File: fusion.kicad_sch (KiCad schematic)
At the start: 67 parts, among them J1 Conn_01x04_Female, J2 USB_C_Receptacle_USB2.0, J3 Conn_02x10_Odd_Even, J4 Conn_02x10_Odd_Even, K1 KEY, K10 KEY, K11 KEY, K12 KEY, K13 KEY, K14 KEY, K15 KEY, K16 KEY, K17 KEY, K18 KEY, K19 KEY, K2 KEY, K20 KEY, K21 KEY, K22 KEY, K23 KEY, K24 KEY, K25 KEY, K26 KEY, K27 KEY, K28 KEY, K29 KEY, K3 KEY, K30 KEY, K31 KEY, K32 KEY, K33 KEY, K34 KEY, K35 KEY, K36 KEY, K37 KEY, K38 KEY, K4 KEY, K5 KEY, K6 KEY, K7 KEY, K8 KEY, K9 KEY, SW1 SW_Push, U1 Holyiot_18010, U2 MT25QL128ABA1ESE, U3 BQ24075, U4 XC6220B331MR, U5 LN4913

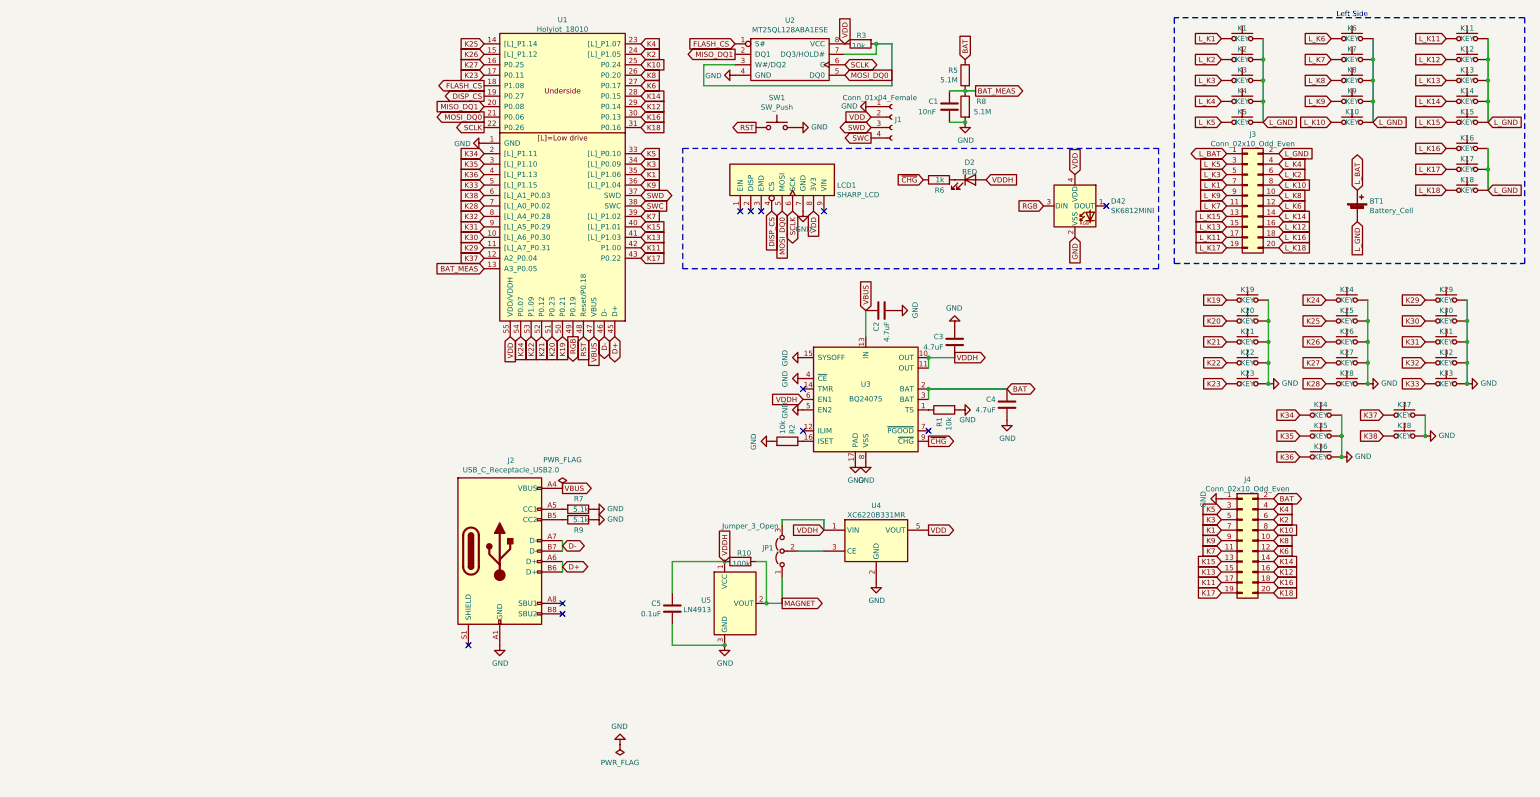
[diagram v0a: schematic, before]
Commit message: fpc and hinges
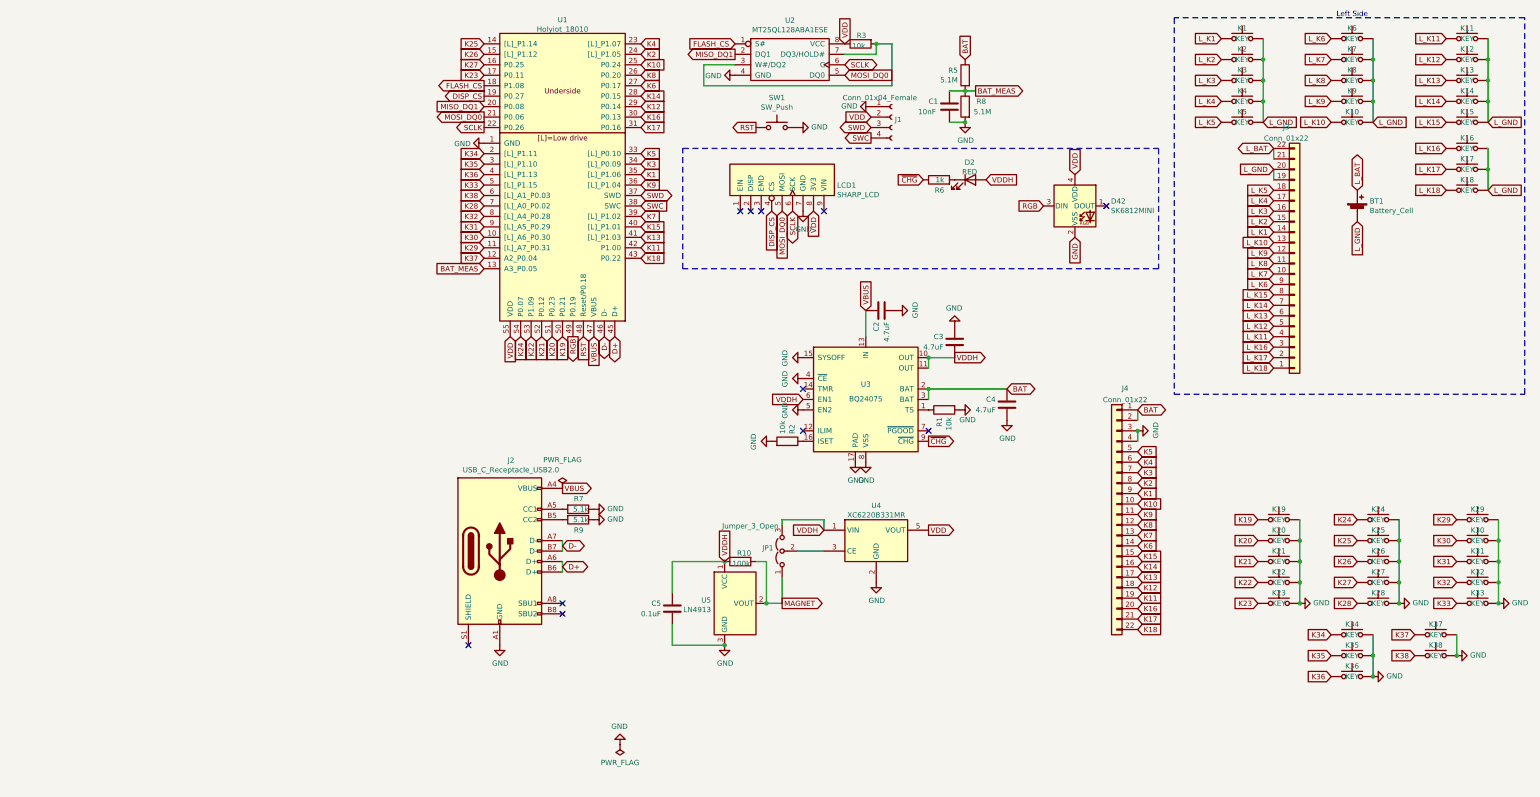
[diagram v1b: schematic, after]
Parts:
- removed J3, J4: Conn_02x10_Odd_Even, Connector_PinHeader_1.27mm:PinHeader_2x10_P1.27mm_Vertical_SMD, symbol Connector_Generic:Conn_02x10_Odd_Even
- added J3, J4: Conn_01x22, Connector_FFC-FPC:Hirose_FH12-22S-0.5SH_1x22-1MP_P0.50mm_Horizontal, symbol Connector_Generic:Conn_01x22
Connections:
- net BAT: now also J4.1 (Pin_1), J4.2 (Pin_2)
- net GND: now also J4.3 (Pin_3), J4.4 (Pin_4)
- net K1: now also J4.9 (Pin_9)
- net K10: now also J4.10 (Pin_10)
- net K11: now also J4.19 (Pin_19)
- net K12: now also J4.18 (Pin_18)
- net K13: now also J4.17 (Pin_17)
- net K14: now also J4.16 (Pin_16)
- net K15: now also J4.15 (Pin_15)
- net K16: now also J4.20 (Pin_20)
- net K17: now also U1.31 (P0.16), J4.21 (Pin_21); no longer U1.43 (P0.22)
- net K18: now also U1.43 (P0.22), J4.22 (Pin_22); no longer U1.31 (P0.16)
- net K2: now also J4.8 (Pin_8)
- net K3: now also J4.7 (Pin_7)
- net K4: now also J4.6 (Pin_6)
- net K5: now also J4.5 (Pin_5)
- net K6: now also J4.14 (Pin_14)
- net K7: now also J4.13 (Pin_13)
- net K8: now also J4.12 (Pin_12)
- net K9: now also J4.11 (Pin_11)
- net L_BAT: now also J3.21 (Pin_21), J3.22 (Pin_22)
- net L_GND: now also J3.19 (Pin_19), J3.20 (Pin_20)
- net L_K1: now also J3.14 (Pin_14)
- net L_K10: now also J3.13 (Pin_13)
- net L_K11: now also J3.4 (Pin_4)
- net L_K12: now also J3.5 (Pin_5)
- net L_K13: now also J3.6 (Pin_6)
- net L_K14: now also J3.7 (Pin_7)
- net L_K15: now also J3.8 (Pin_8)
- net L_K16: now also J3.3 (Pin_3)
- net L_K17: now also J3.2 (Pin_2)
- net L_K18: now also J3.1 (Pin_1)
- net L_K2: now also J3.15 (Pin_15)
- net L_K3: now also J3.16 (Pin_16)
- net L_K4: now also J3.17 (Pin_17)
- net L_K5: now also J3.18 (Pin_18)
- net L_K6: now also J3.9 (Pin_9)
- net L_K7: now also J3.10 (Pin_10)
- net L_K8: now also J3.11 (Pin_11)
- net L_K9: now also J3.12 (Pin_12)
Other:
- moved on the sheet: K19, K20, K21, K22, K23, K24, K25, K26, K27, K28, K29, K30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

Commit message: bug
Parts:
- removed BT1: Battery_Cell, Connector_JST:JST_PH_S2B-PH-K_1x02_P2.00mm_Horizontal, symbol Device:Battery_Cell
- removed C2, C3, C4: 4.7uF, Capacitor_SMD:C_0603_1608Metric, symbol Device:C
- removed C5: 0.1uF, Capacitor_SMD:C_0603_1608Metric, symbol Device:C
- removed D2: RED, LED_SMD:LED_0805_2012Metric, symbol Device:LED
- removed J3, J4: Conn_01x22, Connector_FFC-FPC:Hirose_FH12-22S-0.5SH_1x22-1MP_P0.50mm_Horizontal, symbol Connector_Generic:Conn_01x22
- removed JP1: Jumper_3_Open, Jumper:SolderJumper-3_P2.0mm_Open_TrianglePad1.0x1.5mm_NumberLabels, symbol Jumper:Jumper_3_Open
- removed K1, K10, K11, K15, K37, K38, K5, K6: KEY, keeb-libs:pg1232-shorter-right, symbol Switch:SW_Push
- removed K12, K13, K16, K17, K18, K2, K21, K22, K26, K27, K3, K31, K32, K34, K35, K36, K7, K8: KEY, keeb-libs:pg1232-short, symbol Switch:SW_Push
- removed K14, K4, K9: KEY, keeb-libs:pg1232-short-left, symbol Switch:SW_Push
- removed K19, K23, K24, K28, K29, K33: KEY, keeb-libs:pg1232-shorter-left, symbol Switch:SW_Push
- removed K20, K25, K30: KEY, keeb-libs:pg1232-short-right, symbol Switch:SW_Push
- removed R1, R2: 10k, Resistor_SMD:R_0603_1608Metric, symbol Device:R
- removed R10: 100k, Resistor_SMD:R_0603_1608Metric, symbol Device:R
- removed R6: 1k, Resistor_SMD:R_0603_1608Metric, symbol Device:R
- removed U3: BQ24075, Package_DFN_QFN:VQFN-16-1EP_3x3mm_P0.5mm_EP1.68x1.68mm_ThermalVias, symbol Battery_Management:BQ24075
- removed U4: XC6220B331MR, Package_TO_SOT_SMD:SOT-23-5, symbol Regulator_Linear:XC6220B331MR
- removed U5: LN4913, Package_TO_SOT_SMD:SOT-23, symbol Sensor_Magnetic:A1101ELHL
- added J3, J4: Conn_01x12_MountingPin, Connector_FFC-FPC:Hirose_FH12-12S-0.5SH_1x12-1MP_P0.50mm_Horizontal, symbol Connector_Generic_MountingPin:Conn_01x12_MountingPin
- added J5: trackpad, fusion:trackpad, symbol Connector_Generic:Conn_01x08
- added J6: trackpad_conn, fusion:trackpad_conn, symbol Connector_Generic:Conn_01x08
- added K19, K23, K24, K28, K29, K33: diode-choc, pg1232:pg1232-DSSL, symbol diode-choc:diode-choc
- added K20, K25, K30, K37, K38: diode-choc, pg1232:pg1232-DSSR, symbol diode-choc:diode-choc
- added K21, K22, K26, K27, K31, K32, K34, K35, K36: diode-choc, pg1232:pg1232-DSS, symbol diode-choc:diode-choc
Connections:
- net BAT: now also J4.1 (Pin_1)
- net GND: now also J4.2 (Pin_2), J4.MP (MountPin), J6.2 (Pin_2)
- net MISO_DQ1: now also J6.4 (Pin_4)
- net DISP_CS renamed DISP_~{CS}
- net FLASH_CS renamed FLASH_~{CS}
- net K1 renamed R1
- net R1: now also J4.6 (Pin_6)
- net K10: no longer names the net of U1.25 (P0.24)
- net K11: no longer names the net of U1.42 (P1.00)
- net K12: no longer names the net of U1.29 (P0.14)
- net K13: no longer names the net of U1.41 ([L]_P1.03)
- net K14: no longer names the net of U1.28 (P0.15)
- net K15: no longer names the net of U1.40 ([L]_P1.01)
- net K16: no longer names the net of U1.30 (P0.13)
- net K17: no longer names the net of U1.31 (P0.16)
- net K18: no longer names the net of U1.43 (P0.22)
- net K19 renamed R4
- net R4: now also K19.1, K20.1, K21.1, K22.1, K23.1
- net K2: no longer names the net of U1.24 ([L]_P1.05)
- net K20 renamed R5
- net R5: now also K24.1, K25.1, K26.1, K27.1, K28.1
- net K21 renamed R6
- net R6: now also K29.1, K30.1, K31.1, K32.1, K33.1
- net K22 renamed R7
- net R7: now also K34.1, K35.1, K36.1, K37.1, K38.1
- net K23: no longer names the net of U1.17 (P0.11)
- net K24: no longer names the net of U1.54 (P0.07)
- net K25: no longer names the net of U1.14 ([L]_P1.14)
- net K26: no longer names the net of U1.15 ([L]_P1.12)
- net K27: no longer names the net of U1.16 (P0.25)
- net K28: no longer names the net of U1.7 ([L]_A0_P0.02)
- net K29 renamed MOTION
- net MOTION: now also J6.3 (Pin_3)
- net K3 renamed R2
- net R2: now also J4.5 (Pin_5)
- net K30 renamed TRACKPAD_~{CS}
- net K31: no longer names the net of U1.9 ([L]_A5_P0.29)
- net K32: no longer names the net of U1.8 ([L]_A4_P0.28)
- net K33: no longer names the net of U1.5 ([L]_P1.15)
- net K34: no longer names the net of U1.2 ([L]_P1.11)
- net K35: no longer names the net of U1.3 ([L]_P1.10)
- net K36: no longer names the net of U1.4 ([L]_P1.13)
- net K37 renamed SHTDWN
- net K38: no longer names the net of U1.6 ([L]_A1_P0.03)
- net K4: no longer names the net of U1.23 ([L]_P1.07)
- net K5 renamed R3
- net R3: now also J4.4 (Pin_4)
- net K6: no longer names the net of U1.27 (P0.17)
- net K7: no longer names the net of U1.39 ([L]_P1.02)
- net K8: no longer names the net of U1.26 (P0.20)
- net K9 renamed R0
- net R0: now also J4.7 (Pin_7)
- new net C0: J4.12 (Pin_12), K19.2, K24.2, K29.2, K34.2
- new net C1: J4.11 (Pin_11), K20.2, K25.2, K30.2, K35.2
- new net C2: J4.10 (Pin_10), K21.2, K26.2, K31.2, K36.2
- new net C3: J4.9 (Pin_9), K22.2, K27.2, K32.2, K37.2
- new net C4: J4.8 (Pin_8), K23.2, K28.2, K33.2, K38.2
- new net left/BAT: J3.1 (Pin_1)
- new net left/C0: J3.12 (Pin_12)
- new net left/C1: J3.11 (Pin_11)
- new net left/C2: J3.10 (Pin_10)
- new net left/C3: J3.9 (Pin_9)
- new net left/C4: J3.8 (Pin_8)
- new net left/GND: J3.2 (Pin_2), J3.MP (MountPin)
- new net left/R0: J3.7 (Pin_7)
- new net left/R1: J3.6 (Pin_6)
- new net left/R2: J3.5 (Pin_5)
- new net left/R3: J3.4 (Pin_4)
- new net trackpad/2V8: J5.1 (Pin_1)
- new net trackpad/GND: J5.2 (Pin_2)
- new net trackpad/MISO_2V8: J5.4 (Pin_4)
- new net trackpad/MOSI_2V8: J5.5 (Pin_5)
- new net trackpad/MOTION_2V8: J5.3 (Pin_3)
- new net trackpad/SCK_2V8: J5.6 (Pin_6)
- new net trackpad/SHTDWN_2V8: J5.8 (Pin_8)
- new net trackpad/~{CS}_2V8: J5.7 (Pin_7)
- new net trackpad_conn/2V8: J6.1 (Pin_1)
- new net trackpad_conn/MOSI_2V8: J6.5 (Pin_5)
- new net trackpad_conn/SCK_2V8: J6.6 (Pin_6)
- new net trackpad_conn/SHTDWN_2V8: J6.8 (Pin_8)
- new net trackpad_conn/~{CS}_2V8: J6.7 (Pin_7)
- no-connect marks 11 -> 10
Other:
- added sheet left (left.kicad_sch)
- added sheet power (power.kicad_sch)
- added sheet trackpad (trackpad.kicad_sch)
- added sheet trackpad_conn (trackpad_conn.kicad_sch)
- note removed: "Left Side"
- moved on the sheet: J2, R7, R9

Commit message: trackpad
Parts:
- removed J5: trackpad, fusion:trackpad, symbol Connector_Generic:Conn_01x08
- removed J6: trackpad_conn, fusion:trackpad_conn, symbol Connector_Generic:Conn_01x08
- added H1, H2, H3, H4: trackpad, fusion:trackpad, symbol Mechanical:MountingHole
- added H10, H5, H6, H7, H8, H9: hinge, fusion:hinge, symbol Mechanical:MountingHole
- added H11, H12: hinge-big, fusion:hinge-big, symbol Mechanical:MountingHole
- added H13, H14: hinge-small, fusion:hinge-small, symbol Mechanical:MountingHole
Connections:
- net MOTION: now also U1.12 (A2_P0.04); no longer U1.11 ([L]_A7_P0.31)
- net SHTDWN: now also U1.10 ([L]_A6_P0.30); no longer U1.12 (A2_P0.04)
- net TRACKPAD_~{CS}: now also U1.11 ([L]_A7_P0.31); no longer U1.10 ([L]_A6_P0.30)
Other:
- removed sheet trackpad
- sheet trackpad_conn ports: added MISO_2V8, MOTION_2V8, RST_2V8; removed 2V8, MOSI_2V8, SCK_2V8, SHTDWN_2V8, ~{CS}_2V8
- moved on the sheet: C1, D42, J1, J2, J3, J4, K19, K20, K21, K22, K23, K24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

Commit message: use narrower pinky spacing
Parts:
- K22, K27, K32: footprint pg1232:pg1232-DSS -> pg1232:pg1232-DSSL
- K23, K28, K33: footprint pg1232:pg1232-DSSL -> pg1232:pg1232-DSSN
- K37, K38: footprint pg1232:pg1232-DSSR -> pg1232:pg1232-DSSN
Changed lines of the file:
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@@
       (effects (font (size 1.27 1.27)) (justify left) hide)
     )
-    (property "Footprint" "pg1232:pg1232-DSS" (id 2) (at 205.74 95.25 0)
+    (property "Footprint" "pg1232:pg1232-DSSL" (id 2) (at 205.74 95.25 0)
       (effects (font (size 1.27 1.27)) hide)
     )
@@
       (effects (font (size 1.27 1.27)) (justify left) hide)
     )
-    (property "Footprint" "pg1232:pg1232-DSS" (id 2) (at 205.74 105.41 0)
+    (property "Footprint" "pg1232:pg1232-DSSL" (id 2) (at 205.74 105.41 0)
       (effects (font (size 1.27 1.27)) hide)
     )
@@
       (effects (font (size 1.27 1.27)) (justify left) hide)
     )
-    (property "Footprint" "pg1232:pg1232-DSS" (id 2) (at 205.74 115.57 0)
+    (property "Footprint" "pg1232:pg1232-DSSL" (id 2) (at 205.74 115.57 0)
       (effects (font (size 1.27 1.27)) hide)
     )
@@
       (effects (font (size 1.27 1.27)) (justify left) hide)
     )
-    (property "Footprint" "pg1232:pg1232-DSSR" (id 2) (at 205.74 125.73 0)
+    (property "Footprint" "pg1232:pg1232-DSSN" (id 2) (at 205.74 125.73 0)
       (effects (font (size 1.27 1.27)) hide)
     )
@@
       (effects (font (size 1.27 1.27)) (justify left) hide)
     )
-    (property "Footprint" "pg1232:pg1232-DSSL" (id 2) (at 215.9 95.25 0)
+    (property "Footprint" "pg1232:pg1232-DSSN" (id 2) (at 215.9 95.25 0)
       (effects (font (size 1.27 1.27)) hide)
     )
@@
       (effects (font (size 1.27 1.27)) (justify left) hide)
     )
-    (property "Footprint" "pg1232:pg1232-DSSL" (id 2) (at 215.9 105.41 0)
+    (property "Footprint" "pg1232:pg1232-DSSN" (id 2) (at 215.9 105.41 0)
       (effects (font (size 1.27 1.27)) hide)
     )
@@
       (effects (font (size 1.27 1.27)) (justify left) hide)
     )
-    (property "Footprint" "pg1232:pg1232-DSSL" (id 2) (at 215.9 115.57 0)
+    (property "Footprint" "pg1232:pg1232-DSSN" (id 2) (at 215.9 115.57 0)
       (effects (font (size 1.27 1.27)) hide)
     )
@@
       (effects (font (size 1.27 1.27)) (justify left) hide)
     )
-    (property "Footprint" "pg1232:pg1232-DSSR" (id 2) (at 215.9 125.73 0)
+    (property "Footprint" "pg1232:pg1232-DSSN" (id 2) (at 215.9 125.73 0)
       (effects (font (size 1.27 1.27)) hide)
     )
@@
     )
     (path "/b025309d-e14a-4618-a5e2-fabc6dc93b95/ec8f0ec2-64d7-4a10-99b7-c29746a93bf2"
-      (reference "K1") (unit 1) (value "diode-choc") (footprint "pg1232:pg1232-DSSR")
+      (reference "K1") (unit 1) (value "diode-choc") (footprint "pg1232:pg1232-DSSN")
     )
     (path "/b025309d-e14a-4618-a5e2-fabc6dc93b95/ea55e616-5286-4c86-9c28-1f4fd64101ea"
-      (reference "K2") (unit 1) (value "diode-choc") (footprint "pg1232:pg1232-DSS")
+      (reference "K2") (unit 1) (value "diode-choc") (footprint "pg1232:pg1232-DSSR")
     )
     (path "/b025309d-e14a-4618-a5e2-fabc6dc93b95/dbaba7ab-9e69-492a-aef6-419cd8a9589a"
@@
     )
     (path "/b025309d-e14a-4618-a5e2-fabc6dc93b95/eb00e312-85c3-4881-87de-934f677ff6da"
-      (reference "K6") (unit 1) (value "diode-choc") (footprint "pg1232:pg1232-DSSR")
+      (reference "K6") (unit 1) (value "diode-choc") (footprint "pg1232:pg1232-DSSN")
     )
     (path "/b025309d-e14a-4618-a5e2-fabc6dc93b95/39786762-286c-4388-aea0-bd31a9f816a8"
-      (reference "K7") (unit 1) (value "diode-choc") (footprint "pg1232:pg1232-DSS")
+      (reference "K7") (unit 1) (value "diode-choc") (footprint "pg1232:pg1232-DSSR")
     )
     (path "/b025309d-e14a-4618-a5e2-fabc6dc93b95/b7ab6c15-e56f-4316-a306-8eaffb46142a"
@@
     )
     (path "/b025309d-e14a-4618-a5e2-fabc6dc93b95/37f8abae-7333-43fb-99a4-da93acedc704"
-      (reference "K11") (unit 1) (value "diode-choc") (footprint "pg1232:pg1232-DSSR")
+      (reference "K11") (unit 1) (value "diode-choc") (footprint "pg1232:pg1232-DSSN")
     )
     (path "/b025309d-e14a-4618-a5e2-fabc6dc93b95/68e20e26-32a0-4290-994f-29c8ee51c370"
-      (reference "K12") (unit 1) (value "diode-choc") (footprint "pg1232:pg1232-DSS")
+      (reference "K12") (unit 1) (value "diode-choc") (footprint "pg1232:pg1232-DSSR")
     )
     (path "/b025309d-e14a-4618-a5e2-fabc6dc93b95/761f5148-54d9-40e5-afe0-bb083f7aebe2"
@@
     )
     (path "/a2751d21-116d-4919-a086-ff623395a909"
-      (reference "K22") (unit 1) (value "diode-choc") (footprint "pg1232:pg1232-DSS")
+      (reference "K22") (unit 1) (value "diode-choc") (footprint "pg1232:pg1232-DSSL")
     )
     (path "/e0276649-86b3-489f-adee-25773aff83dd"
-      (reference "K23") (unit 1) (value "diode-choc") (footprint "pg1232:pg1232-DSSL")
+      (reference "K23") (unit 1) (value "diode-choc") (footprint "pg1232:pg1232-DSSN")
     )
     (path "/9f3fa4fe-5952-4a9d-bdcf-1cc867e9f28e"
@@
     )
     (path "/c0724dd3-1150-4fa2-8615-6c3c918d177f"
-      (reference "K27") (unit 1) (value "diode-choc") (footprint "pg1232:pg1232-DSS")
+      (reference "K27") (unit 1) (value "diode-choc") (footprint "pg1232:pg1232-DSSL")
     )
     (path "/b2f94a00-b47b-457b-b67a-ebf74ff78fd0"
-      (reference "K28") (unit 1) (value "diode-choc") (footprint "pg1232:pg1232-DSSL")
+      (reference "K28") (unit 1) (value "diode-choc") (footprint "pg1232:pg1232-DSSN")
     )
     (path "/588b9435-5c8c-4b21-b648-6a2c93badb70"
@@
     )
     (path "/08860645-1a04-42cc-86a1-71433fbebf2d"
-      (reference "K32") (unit 1) (value "diode-choc") (footprint "pg1232:pg1232-DSS")
+      (reference "K32") (unit 1) (value "diode-choc") (footprint "pg1232:pg1232-DSSL")
     )
     (path "/6693fc87-39b5-4df2-96fc-bb16e0f26ce7"
-      (reference "K33") (unit 1) (value "diode-choc") (footprint "pg1232:pg1232-DSSL")
+      (reference "K33") (unit 1) (value "diode-choc") (footprint "pg1232:pg1232-DSSN")
     )
     (path "/0a5613c6-21cf-4887-8e46-b7c8bc527b5d"
@@
     )
     (path "/175e3bc8-bf50-4f06-bba6-540b3a2a2eae"
-      (reference "K37") (unit 1) (value "diode-choc") (footprint "pg1232:pg1232-DSSR")
+      (reference "K37") (unit 1) (value "diode-choc") (footprint "pg1232:pg1232-DSSN")
     )
     (path "/3f566f17-ccaa-4d39-a0ab-0258a2b72084"
-      (reference "K38") (unit 1) (value "diode-choc") (footprint "pg1232:pg1232-DSSR")
+      (reference "K38") (unit 1) (value "diode-choc") (footprint "pg1232:pg1232-DSSN")
     )
     (path "/60cf3122-165f-4c8f-8410-6cfec7ab4ce2"
